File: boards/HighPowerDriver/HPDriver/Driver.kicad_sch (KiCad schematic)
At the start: 33 parts, among them Q1 IRFR5410, Q2 IRFR3910, Q3 IRFR3910, Q4 IRFR5410, Q5 IRFR5410, Q6 IRFR3910, Q7 IRFR3910, Q8 IRFR5410, U2 TMC262, X1 16MHz

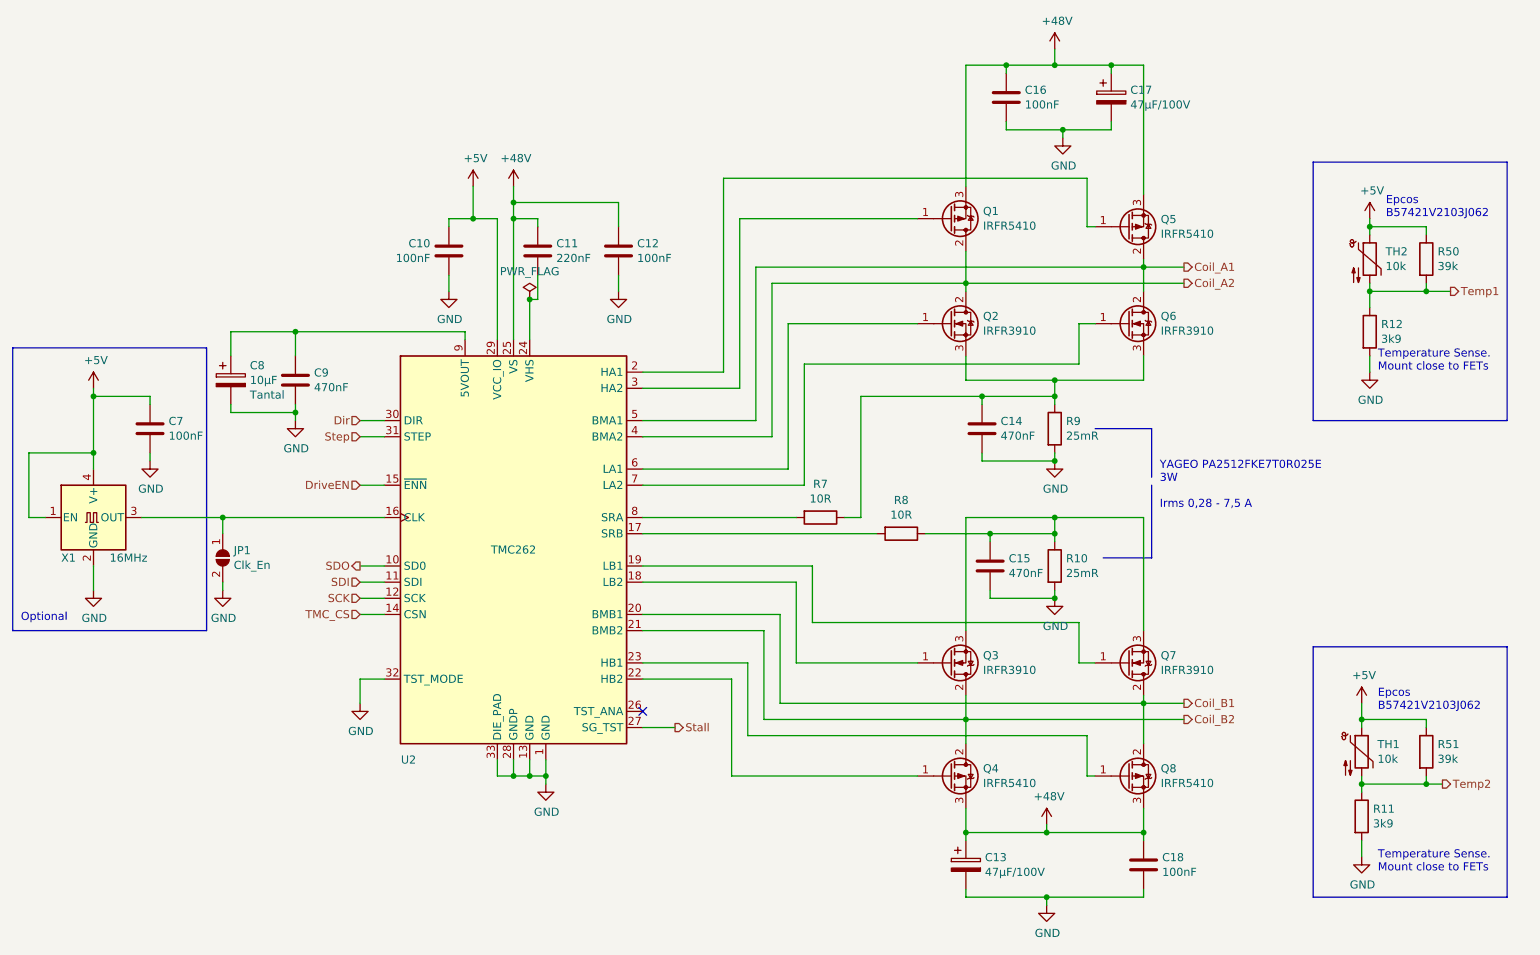
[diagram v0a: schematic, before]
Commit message: Changed Controller to ATmega328PB
The ATtiny did not have enough flash
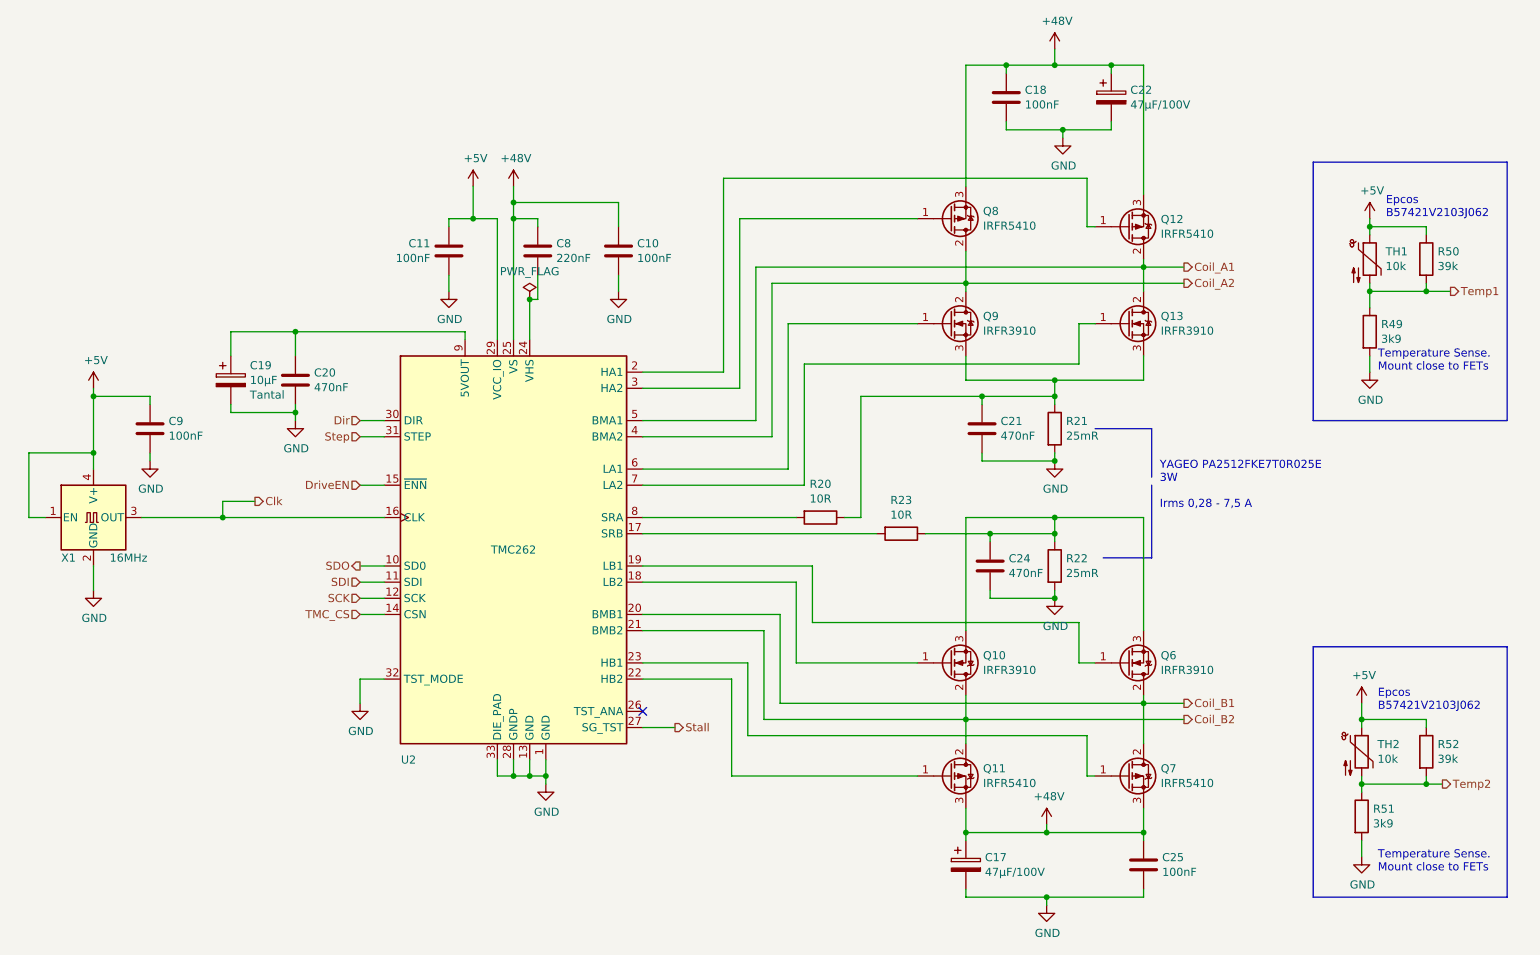
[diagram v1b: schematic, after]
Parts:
- removed JP1: Clk_En, Jumper:SolderJumper-2_P1.3mm_Open_TrianglePad1.0x1.5mm, symbol Jumper:SolderJumper_2_Open
- renumbered C12 to C10, C10 to C11, C13 to C17, C16 to C18, C8 to C19, C9 to C20, C14 to C21, C17 to C22, C15 to C24, C18 to C25, C11 to C8, C7 to C9, Q3 to Q10, Q4 to Q11, Q5 to Q12, Q6 to Q13, Q7 to Q6, Q8 to Q7, Q1 to Q8, Q2 to Q9, R7 to R20, R9 to R21, R10 to R22, R8 to R23, R12 to R49, R11 to R51, R51 to R52, TH2 to TH1, TH1 to TH2
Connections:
- net Clk: now reaches U2.16 (CLK), X1.3 (OUT)
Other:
- note removed: "Optional"
